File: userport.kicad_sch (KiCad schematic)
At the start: 13 parts, among them J17 C64_Tape_Port, J18 BA60BC0WT, J19 C64_User_Port, U16 74LVC374, U17 74LVC374, U18 74LS374, U19 74LS374, U20 74LS125, U21 74LS125, U23 74LVC374, U24 74LS125, U25 74LS374, U26 74LS374

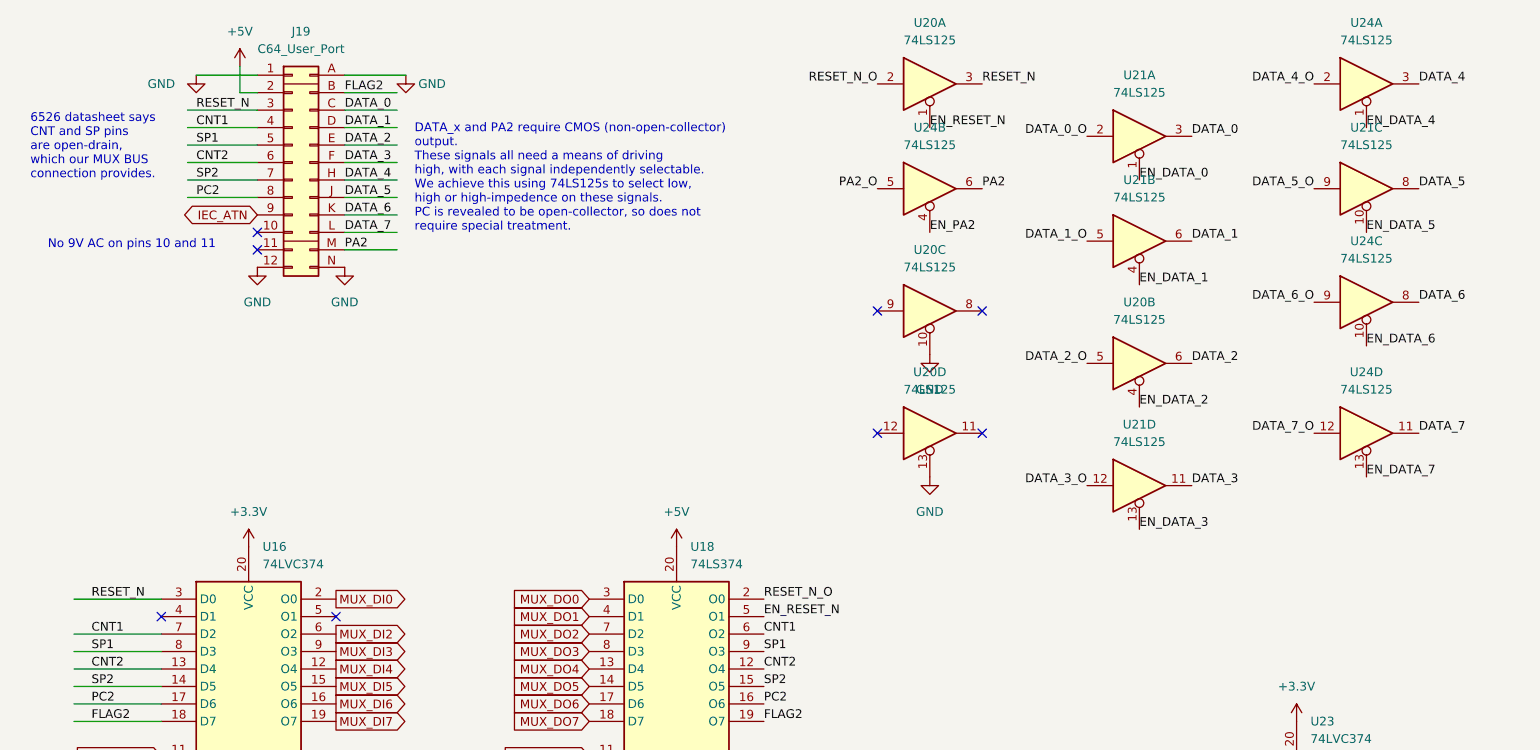
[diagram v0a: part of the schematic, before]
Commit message: work on routing user port
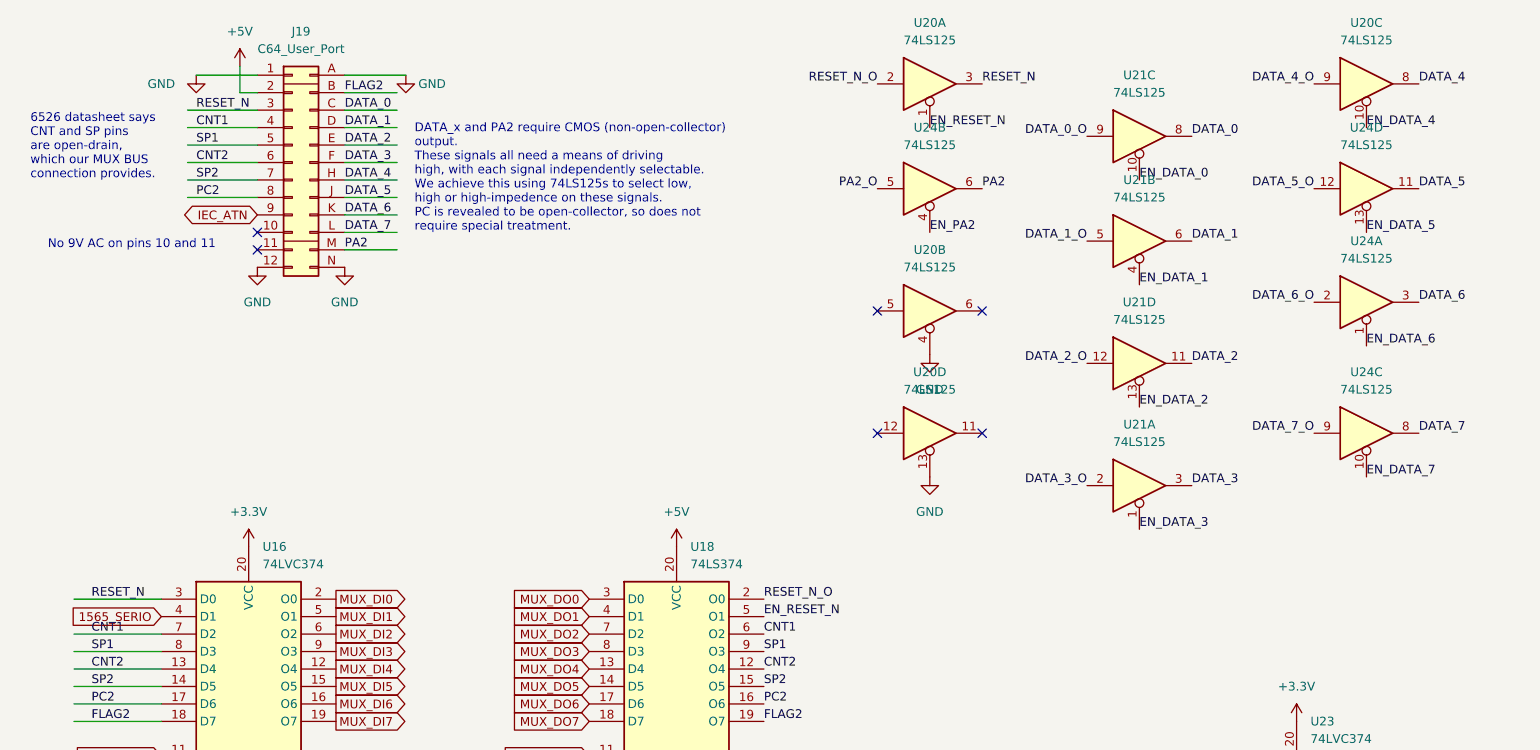
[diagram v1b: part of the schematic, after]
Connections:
- net DATA_0: now also U21.8; no longer U21.3
- net DATA_0_O: now also U21.9; no longer U21.2
- net DATA_2: now also U21.11; no longer U20.6
- net DATA_2_O: now also U21.12; no longer U20.5
- net DATA_3: now also U21.3; no longer U21.11
- net DATA_3_O: now also U21.2; no longer U21.12
- net DATA_4: now also U20.8; no longer U24.3
- net DATA_4_O: now also U20.9; no longer U24.2
- net DATA_5: now also U24.11; no longer U21.8
- net DATA_5_O: now also U24.12; no longer U21.9
- net DATA_6: now also U24.3; no longer U24.8
- net DATA_6_O: now also U24.2; no longer U24.9
- net DATA_7: now also U24.8; no longer U24.11
- net DATA_7_O: now also U24.9; no longer U24.12
- net EN_DATA_0: now also U21.10; no longer U21.1
- net EN_DATA_2: now also U21.13; no longer U20.4
- net EN_DATA_3: now also U21.1; no longer U21.13
- net EN_DATA_4: now also U20.10; no longer U24.1
- net EN_DATA_5: now also U24.13; no longer U21.10
- net EN_DATA_6: now also U24.1; no longer U24.10
- net EN_DATA_7: now also U24.10; no longer U24.13
- net GND: now also U20.4; no longer U20.10
- net MUX_DI1: now also U16.5 (O1)
- net 1565_SERIO: now reaches U16.4 (D1)
- no-connect marks 11 -> 9
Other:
- moved on the sheet: U20B, U20C, U21A, U21C, U21D, U24A, U24C, U24D

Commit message: more routing
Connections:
- net DATA_0_O: now also U26.12 (O4); no longer U26.2 (O0)
- net DATA_2_O: now also U26.9 (O3); no longer U26.6 (O2)
- net DATA_3_O: now also U26.6 (O2); no longer U26.9 (O3)
- net DATA_4_O: now also U26.2 (O0); no longer U26.12 (O4)
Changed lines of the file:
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@@
     (effects (font (size 1.27 1.27)) (justify left bottom))
   )
-  (label "DATA_0_O" (at 271.78 123.19 0)
+  (label "DATA_0_O" (at 271.78 133.35 0)
     (effects (font (size 1.27 1.27)) (justify left bottom))
   )
@@
     (effects (font (size 1.27 1.27)) (justify left bottom))
   )
-  (label "DATA_2_O" (at 271.78 128.27 0)
+  (label "DATA_2_O" (at 271.78 130.81 0)
     (effects (font (size 1.27 1.27)) (justify left bottom))
   )
@@
     (effects (font (size 1.27 1.27)) (justify left bottom))
   )
-  (label "DATA_3_O" (at 271.78 130.81 0)
+  (label "DATA_3_O" (at 271.78 128.27 0)
     (effects (font (size 1.27 1.27)) (justify left bottom))
   )
@@
     (effects (font (size 1.27 1.27)) (justify left bottom))
   )
-  (label "DATA_4_O" (at 271.78 133.35 0)
+  (label "DATA_4_O" (at 271.78 123.19 0)
     (effects (font (size 1.27 1.27)) (justify left bottom))
   )

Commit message: add footprints to differentiate 3.3V from 5V ICs
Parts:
- U16, U17, U23: footprint Package_DIP:DIP-20_W7.62mm -> snapeda:DIP-20_LVC_Family
- U18, U19, U25, U26: footprint Package_DIP:DIP-20_W7.62mm -> snapeda:DIP-20_LS_Family
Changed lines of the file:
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@@
       (effects (font (size 1.27 1.27)) (justify left))
     )
-    (property "Footprint" "Package_DIP:DIP-20_W7.62mm" (id 2) (at 143.51 168.91 0)
+    (property "Footprint" "snapeda:DIP-20_LS_Family" (id 2) (at 143.51 168.91 0)
       (effects (font (size 1.27 1.27)) hide)
     )
@@
       (effects (font (size 1.27 1.27)) (justify left))
     )
-    (property "Footprint" "Package_DIP:DIP-20_W7.62mm" (id 2) (at 45.72 110.49 0)
+    (property "Footprint" "snapeda:DIP-20_LVC_Family" (id 2) (at 45.72 110.49 0)
       (effects (font (size 1.27 1.27)) hide)
     )
@@
       (effects (font (size 1.27 1.27)) (justify left))
     )
-    (property "Footprint" "Package_DIP:DIP-20_W7.62mm" (id 2) (at 259.08 135.89 0)
+    (property "Footprint" "snapeda:DIP-20_LS_Family" (id 2) (at 259.08 135.89 0)
       (effects (font (size 1.27 1.27)) hide)
     )
@@
       (effects (font (size 1.27 1.27)) (justify left))
     )
-    (property "Footprint" "Package_DIP:DIP-20_W7.62mm" (id 2) (at 107.95 110.49 0)
+    (property "Footprint" "snapeda:DIP-20_LS_Family" (id 2) (at 107.95 110.49 0)
       (effects (font (size 1.27 1.27)) hide)
     )
@@
       (effects (font (size 1.27 1.27)) (justify left))
     )
-    (property "Footprint" "Package_DIP:DIP-20_W7.62mm" (id 2) (at 259.08 78.74 0)
+    (property "Footprint" "snapeda:DIP-20_LS_Family" (id 2) (at 259.08 78.74 0)
       (effects (font (size 1.27 1.27)) hide)
     )
@@
       (effects (font (size 1.27 1.27)) (justify left))
     )
-    (property "Footprint" "Package_DIP:DIP-20_W7.62mm" (id 2) (at 87.63 168.91 0)
+    (property "Footprint" "snapeda:DIP-20_LVC_Family" (id 2) (at 87.63 168.91 0)
       (effects (font (size 1.27 1.27)) hide)
     )
@@
       (effects (font (size 1.27 1.27)) (justify left))
     )
-    (property "Footprint" "Package_DIP:DIP-20_W7.62mm" (id 2) (at 198.12 135.89 0)
-      (effects (font (size 1.27 1.27)) hide)
-    )
+    (property "Footprint" "snapeda:DIP-20_LVC_Family" (id 2) (at 198.12 135.89 0)
+      (effects (font (size 1.27 1.27)) hide)
+    )

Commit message: re-do many labels and DRC fixes
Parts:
- U20, U21, U24: footprint Package_DIP:DIP-14_W7.62mm -> snapeda:DIP-14_74LS06
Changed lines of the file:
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@@
     (property "Reference" "U21" (id 0) (at 175.26 54.61 0))
     (property "Value" "74LS125" (id 1) (at 175.26 57.15 0))
-    (property "Footprint" "Package_DIP:DIP-14_W7.62mm" (id 2) (at 175.26 63.5 0)
+    (property "Footprint" "snapeda:DIP-14_74LS06" (id 2) (at 175.26 63.5 0)
       (effects (font (size 1.27 1.27)) hide)
     )
@@
     (property "Reference" "U24" (id 0) (at 144.78 29.21 0))
     (property "Value" "74LS125" (id 1) (at 144.78 31.75 0))
-    (property "Footprint" "Package_DIP:DIP-14_W7.62mm" (id 2) (at 144.78 38.1 0)
+    (property "Footprint" "snapeda:DIP-14_74LS06" (id 2) (at 144.78 38.1 0)
       (effects (font (size 1.27 1.27)) hide)
     )
@@
     (property "Reference" "U21" (id 0) (at 175.26 72.39 0))
     (property "Value" "74LS125" (id 1) (at 175.26 74.93 0))
-    (property "Footprint" "Package_DIP:DIP-14_W7.62mm" (id 2) (at 175.26 81.28 0)
+    (property "Footprint" "snapeda:DIP-14_74LS06" (id 2) (at 175.26 81.28 0)
       (effects (font (size 1.27 1.27)) hide)
     )
@@
     (property "Reference" "U20" (id 0) (at 144.78 13.97 0))
     (property "Value" "74LS125" (id 1) (at 144.78 16.51 0))
-    (property "Footprint" "Package_DIP:DIP-14_W7.62mm" (id 2) (at 144.78 22.86 0)
+    (property "Footprint" "snapeda:DIP-14_74LS06" (id 2) (at 144.78 22.86 0)
       (effects (font (size 1.27 1.27)) hide)
     )
@@
       (effects (font (size 1.27 1.27)) (justify left))
     )
-    (property "Footprint" "Package_DIP:DIP-14_W7.62mm" (id 2) (at 246.38 36.83 0)
+    (property "Footprint" "snapeda:DIP-14_74LS06" (id 2) (at 246.38 36.83 0)
       (effects (font (size 1.27 1.27)) hide)
     )
@@
     (property "Reference" "U20" (id 0) (at 144.78 64.77 0))
     (property "Value" "74LS125" (id 1) (at 144.78 67.31 0))
-    (property "Footprint" "Package_DIP:DIP-14_W7.62mm" (id 2) (at 144.78 73.66 0)
+    (property "Footprint" "snapeda:DIP-14_74LS06" (id 2) (at 144.78 73.66 0)
       (effects (font (size 1.27 1.27)) hide)
     )
@@
     (property "Reference" "U21" (id 0) (at 175.26 21.59 0))
     (property "Value" "74LS125" (id 1) (at 175.26 24.13 0))
-    (property "Footprint" "Package_DIP:DIP-14_W7.62mm" (id 2) (at 175.26 30.48 0)
+    (property "Footprint" "snapeda:DIP-14_74LS06" (id 2) (at 175.26 30.48 0)
       (effects (font (size 1.27 1.27)) hide)
     )
@@
     (property "Reference" "U20" (id 0) (at 144.78 46.99 0))
     (property "Value" "74LS125" (id 1) (at 144.78 49.53 0))
-    (property "Footprint" "Package_DIP:DIP-14_W7.62mm" (id 2) (at 144.78 55.88 0)
+    (property "Footprint" "snapeda:DIP-14_74LS06" (id 2) (at 144.78 55.88 0)
       (effects (font (size 1.27 1.27)) hide)
     )
@@
       (effects (font (size 1.27 1.27)) (justify left))
     )
-    (property "Footprint" "Package_DIP:DIP-14_W7.62mm" (id 2) (at 271.78 36.83 0)
+    (property "Footprint" "snapeda:DIP-14_74LS06" (id 2) (at 271.78 36.83 0)
       (effects (font (size 1.27 1.27)) hide)
     )
@@
     (property "Reference" "U24" (id 0) (at 208.28 45.72 0))
     (property "Value" "74LS125" (id 1) (at 208.28 48.26 0))
-    (property "Footprint" "Package_DIP:DIP-14_W7.62mm" (id 2) (at 208.28 54.61 0)
+    (property "Footprint" "snapeda:DIP-14_74LS06" (id 2) (at 208.28 54.61 0)
       (effects (font (size 1.27 1.27)) hide)
     )
@@
     (property "Reference" "U21" (id 0) (at 175.26 36.83 0))
     (property "Value" "74LS125" (id 1) (at 175.26 39.37 0))
-    (property "Footprint" "Package_DIP:DIP-14_W7.62mm" (id 2) (at 175.26 45.72 0)
+    (property "Footprint" "snapeda:DIP-14_74LS06" (id 2) (at 175.26 45.72 0)
       (effects (font (size 1.27 1.27)) hide)
     )
@@
     (property "Reference" "U20" (id 0) (at 208.28 13.97 0))
     (property "Value" "74LS125" (id 1) (at 208.28 16.51 0))
-    (property "Footprint" "Package_DIP:DIP-14_W7.62mm" (id 2) (at 208.28 22.86 0)
+    (property "Footprint" "snapeda:DIP-14_74LS06" (id 2) (at 208.28 22.86 0)
       (effects (font (size 1.27 1.27)) hide)
     )
@@
       (effects (font (size 1.27 1.27)) (justify left))
     )
-    (property "Footprint" "Package_DIP:DIP-14_W7.62mm" (id 2) (at 259.08 36.83 0)
+    (property "Footprint" "snapeda:DIP-14_74LS06" (id 2) (at 259.08 36.83 0)
       (effects (font (size 1.27 1.27)) hide)
     )
@@
     (property "Reference" "U24" (id 0) (at 208.28 64.77 0))
     (property "Value" "74LS125" (id 1) (at 208.28 67.31 0))
-    (property "Footprint" "Package_DIP:DIP-14_W7.62mm" (id 2) (at 208.28 73.66 0)
+    (property "Footprint" "snapeda:DIP-14_74LS06" (id 2) (at 208.28 73.66 0)
       (effects (font (size 1.27 1.27)) hide)
     )
@@
     (property "Reference" "U24" (id 0) (at 208.28 29.21 0))
     (property "Value" "74LS125" (id 1) (at 208.28 31.75 0))
-    (property "Footprint" "Package_DIP:DIP-14_W7.62mm" (id 2) (at 208.28 38.1 0)
-      (effects (font (size 1.27 1.27)) hide)
-    )
+    (property "Footprint" "snapeda:DIP-14_74LS06" (id 2) (at 208.28 38.1 0)
+      (effects (font (size 1.27 1.27)) hide)
+    )
